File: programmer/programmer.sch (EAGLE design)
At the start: 5 parts

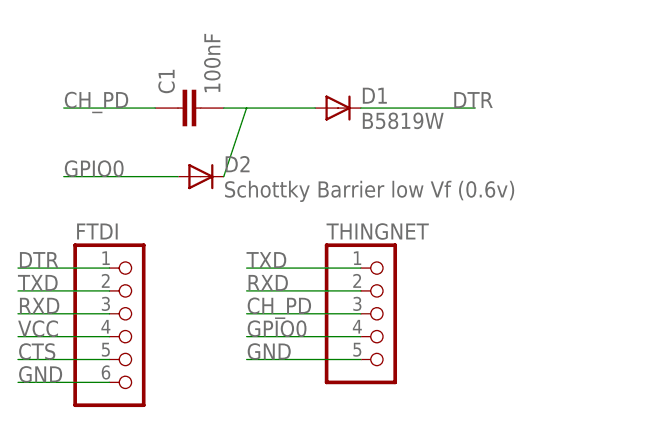
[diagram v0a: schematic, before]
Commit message: Updated programmer board and organized everything into folders
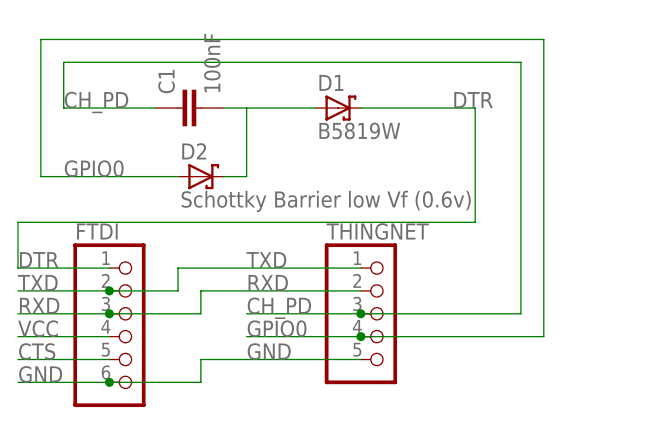
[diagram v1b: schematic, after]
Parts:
- D1, D2: device diode:DIODE-D-5 -> diode:SCHOTTKY-DIODEDO35-7
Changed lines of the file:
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@@
 <parts>
 <part name="THINGNET" library="pinhead" deviceset="PINHD-1X5" device=""/>
-<part name="D1" library="diode" deviceset="DIODE-" device="D-5" value="B5819W"/>
-<part name="D2" library="diode" deviceset="DIODE-" device="D-5" value="Schottky Barrier low Vf (0.6v)"/>
+<part name="D1" library="diode" deviceset="SCHOTTKY-DIODE" device="DO35-7" value="B5819W"/>
+<part name="D2" library="diode" deviceset="SCHOTTKY-DIODE" device="DO35-7" value="Schottky Barrier low Vf (0.6v)"/>
 <part name="C1" library="rcl" deviceset="C-EU" device="025-024X044" value="100nF"/>
 <part name="FTDI" library="pinhead" deviceset="PINHD-1X6" device=""/>
@@
 <net name="GND" class="0">
 <segment>
-<pinref part="THINGNET" gate="A" pin="5"/>
-<wire x1="99.06" y1="93.98" x2="86.36" y2="93.98" width="0.1524" layer="91"/>
-<label x="86.36" y="93.98" size="1.778" layer="95"/>
-</segment>
-<segment>
 <pinref part="FTDI" gate="A" pin="6"/>
 <wire x1="71.12" y1="91.44" x2="60.96" y2="91.44" width="0.1524" layer="91"/>
 <label x="60.96" y="91.44" size="1.778" layer="95"/>
+<wire x1="71.12" y1="91.44" x2="81.28" y2="91.44" width="0.1524" layer="91"/>
+<wire x1="81.28" y1="91.44" x2="81.28" y2="93.98" width="0.1524" layer="91"/>
+<junction x="71.12" y="91.44"/>
+<pinref part="THINGNET" gate="A" pin="5"/>
+<wire x1="99.06" y1="93.98" x2="81.28" y2="93.98" width="0.1524" layer="91"/>
+<label x="86.36" y="93.98" size="1.778" layer="95"/>
 </segment>
 </net>
 <net name="TXD" class="0">
 <segment>
-<wire x1="99.06" y1="104.14" x2="86.36" y2="104.14" width="0.1524" layer="91"/>
-<label x="86.36" y="104.14" size="1.778" layer="95"/>
-<pinref part="THINGNET" gate="A" pin="1"/>
-</segment>
-<segment>
 <pinref part="FTDI" gate="A" pin="2"/>
 <wire x1="71.12" y1="101.6" x2="60.96" y2="101.6" width="0.1524" layer="91"/>
 <label x="60.96" y="101.6" size="1.778" layer="95"/>
+<wire x1="71.12" y1="101.6" x2="78.74" y2="101.6" width="0.1524" layer="91"/>
+<wire x1="78.74" y1="101.6" x2="78.74" y2="104.14" width="0.1524" layer="91"/>
+<junction x="71.12" y="101.6"/>
+<wire x1="99.06" y1="104.14" x2="78.74" y2="104.14" width="0.1524" layer="91"/>
+<label x="86.36" y="104.14" size="1.778" layer="95"/>
+<pinref part="THINGNET" gate="A" pin="1"/>
 </segment>
 </net>
 <net name="RXD" class="0">
 <segment>
-<wire x1="99.06" y1="101.6" x2="86.36" y2="101.6" width="0.1524" layer="91"/>
-<label x="86.36" y="101.6" size="1.778" layer="95"/>
-<pinref part="THINGNET" gate="A" pin="2"/>
-</segment>
-<segment>
 <pinref part="FTDI" gate="A" pin="3"/>
 <wire x1="71.12" y1="99.06" x2="60.96" y2="99.06" width="0.1524" layer="91"/>
 <label x="60.96" y="99.06" size="1.778" layer="95"/>
+<wire x1="71.12" y1="99.06" x2="81.28" y2="99.06" width="0.1524" layer="91"/>
+<wire x1="81.28" y1="99.06" x2="81.28" y2="101.6" width="0.1524" layer="91"/>
+<junction x="71.12" y="99.06"/>
+<wire x1="99.06" y1="101.6" x2="81.28" y2="101.6" width="0.1524" layer="91"/>
+<label x="86.36" y="101.6" size="1.778" layer="95"/>
+<pinref part="THINGNET" gate="A" pin="2"/>
 </segment>
 </net>
@@
 <label x="86.36" y="96.52" size="1.778" layer="95"/>
 <pinref part="THINGNET" gate="A" pin="4"/>
-</segment>
-<segment>
-<wire x1="78.74" y1="114.3" x2="66.04" y2="114.3" width="0.1524" layer="91"/>
+<wire x1="99.06" y1="96.52" x2="119.38" y2="96.52" width="0.1524" layer="91"/>
+<wire x1="119.38" y1="96.52" x2="119.38" y2="129.54" width="0.1524" layer="91"/>
+<junction x="99.06" y="96.52"/>
+<wire x1="119.38" y1="129.54" x2="63.5" y2="129.54" width="0.1524" layer="91"/>
+<wire x1="63.5" y1="129.54" x2="63.5" y2="114.3" width="0.1524" layer="91"/>
+<wire x1="78.74" y1="114.3" x2="63.5" y2="114.3" width="0.1524" layer="91"/>
 <label x="66.04" y="114.3" size="1.778" layer="95"/>
 <pinref part="D2" gate="G$1" pin="A"/>
@@
 <wire x1="86.36" y1="99.06" x2="99.06" y2="99.06" width="0.1524" layer="91"/>
 <label x="86.36" y="99.06" size="1.778" layer="95"/>
-</segment>
-<segment>
+<wire x1="99.06" y1="99.06" x2="116.84" y2="99.06" width="0.1524" layer="91"/>
+<wire x1="116.84" y1="99.06" x2="116.84" y2="127" width="0.1524" layer="91"/>
+<junction x="99.06" y="99.06"/>
 <pinref part="C1" gate="G$1" pin="1"/>
 <wire x1="76.2" y1="121.92" x2="66.04" y2="121.92" width="0.1524" layer="91"/>
 <label x="66.04" y="121.92" size="1.778" layer="95"/>
+<wire x1="116.84" y1="127" x2="66.04" y2="127" width="0.1524" layer="91"/>
+<wire x1="66.04" y1="127" x2="66.04" y2="121.92" width="0.1524" layer="91"/>
 </segment>
 </net>
 <net name="DTR" class="0">
 <segment>
+<pinref part="FTDI" gate="A" pin="1"/>
+<wire x1="71.12" y1="104.14" x2="60.96" y2="104.14" width="0.1524" layer="91"/>
+<label x="60.96" y="104.14" size="1.778" layer="95"/>
+<wire x1="60.96" y1="104.14" x2="60.96" y2="109.22" width="0.1524" layer="91"/>
 <wire x1="111.76" y1="121.92" x2="99.06" y2="121.92" width="0.1524" layer="91"/>
 <pinref part="D1" gate="G$1" pin="C"/>
 <label x="109.22" y="121.92" size="1.778" layer="95"/>
-</segment>
-<segment>
-<pinref part="FTDI" gate="A" pin="1"/>
-<wire x1="71.12" y1="104.14" x2="60.96" y2="104.14" width="0.1524" layer="91"/>
-<label x="60.96" y="104.14" size="1.778" layer="95"/>
+<wire x1="60.96" y1="109.22" x2="111.76" y2="109.22" width="0.1524" layer="91"/>
+<wire x1="111.76" y1="109.22" x2="111.76" y2="121.92" width="0.1524" layer="91"/>
 </segment>
 </net>
@@
 <segment>
 <wire x1="93.98" y1="121.92" x2="86.36" y2="121.92" width="0.1524" layer="91"/>
-<wire x1="86.36" y1="121.92" x2="83.82" y2="114.3" width="0.1524" layer="91"/>
+<wire x1="86.36" y1="121.92" x2="86.36" y2="114.3" width="0.1524" layer="91"/>
+<wire x1="86.36" y1="114.3" x2="83.82" y2="114.3" width="0.1524" layer="91"/>
 <pinref part="C1" gate="G$1" pin="2"/>
 <wire x1="86.36" y1="121.92" x2="83.82" y2="121.92" width="0.1524" layer="91"/>
